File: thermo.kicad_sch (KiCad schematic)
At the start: 39 parts, among them J1 USB_C_Receptacle_USB2.0_14P, Q1 NPN, Q2 NPN, U1 ESP32-C6, U2 W25Q128JVS, U3 USBLC6-2SC6, Y1 40M, Y2 32k768

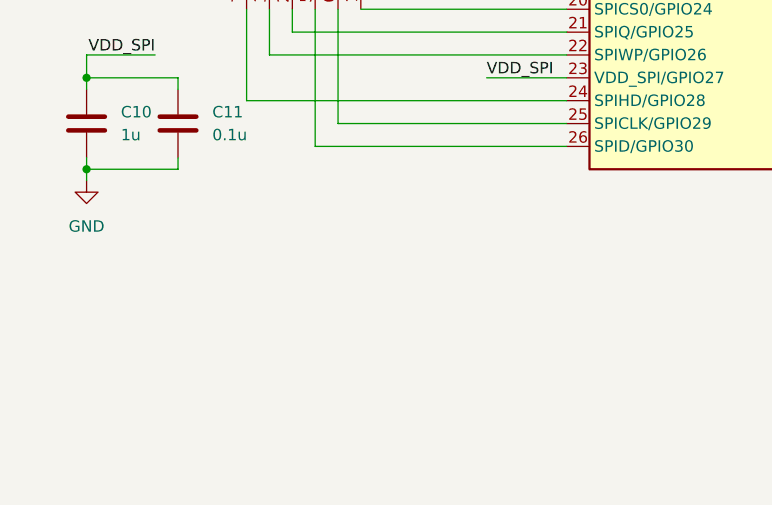
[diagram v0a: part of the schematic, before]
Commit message: add 5v to 3v3 ldo
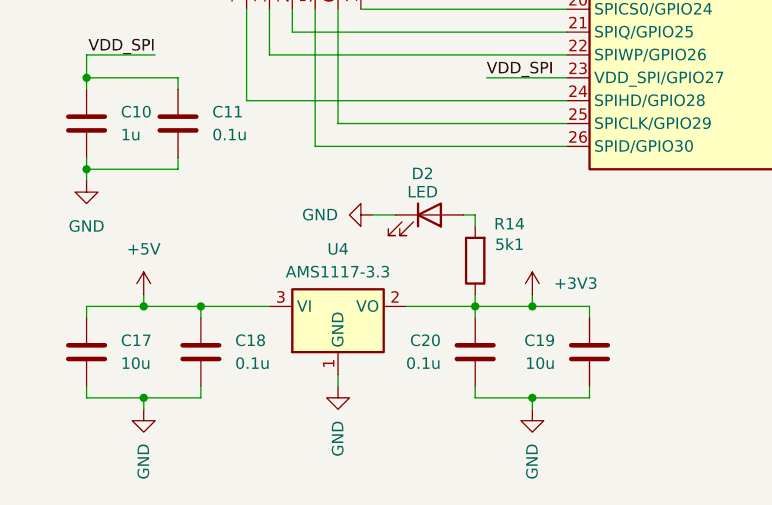
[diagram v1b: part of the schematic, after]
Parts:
- added C17, C19: 10u, symbol Device:C
- added C18, C20: 0.1u, symbol Device:C
- added D2: LED, symbol Device:LED
- added R14: 5k1, symbol Device:R
- added U4: AMS1117-3.3, Package_TO_SOT_SMD:SOT-223-3_TabPin2, symbol Regulator_Linear:AMS1117-3.3
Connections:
- net +3V3: now also C19.1, C20.1, R14.1, U4.2 (VO)
- net +5V: now also C17.1, C18.1, U4.3 (VI)
- net GND: now also C17.2, C18.2, C19.2, C20.2, D2.1 (K), U4.1 (GND)
- new net: D2.2 (A), R14.2

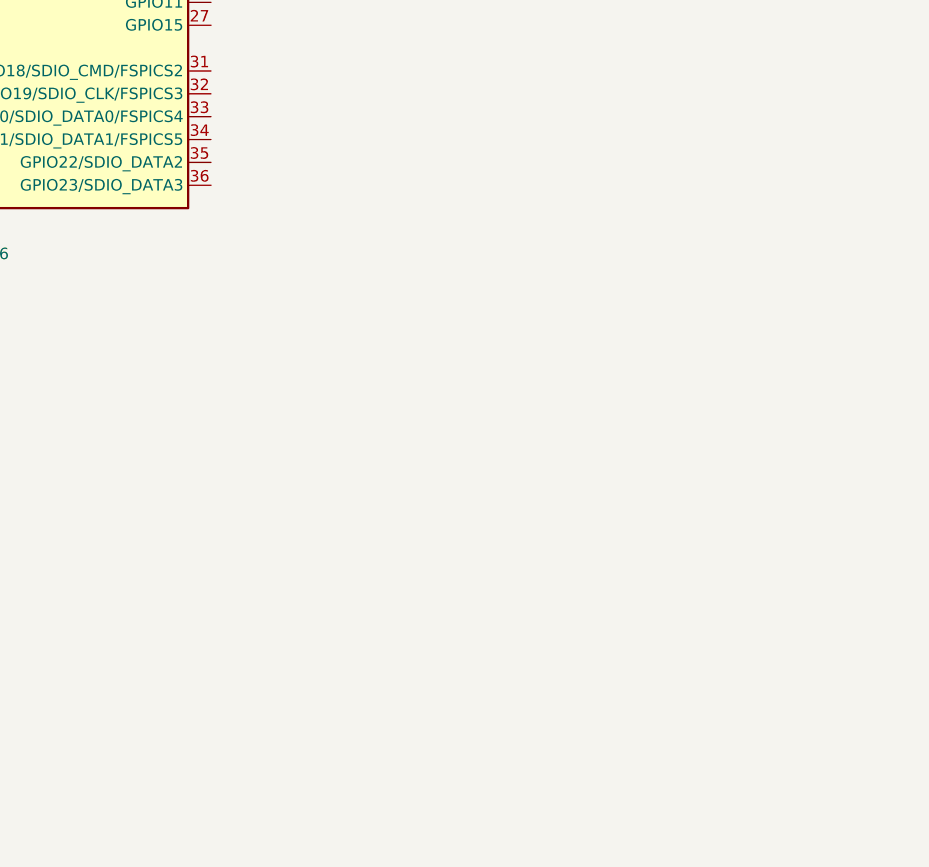
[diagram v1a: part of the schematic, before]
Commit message: add CP2102N usb to uart
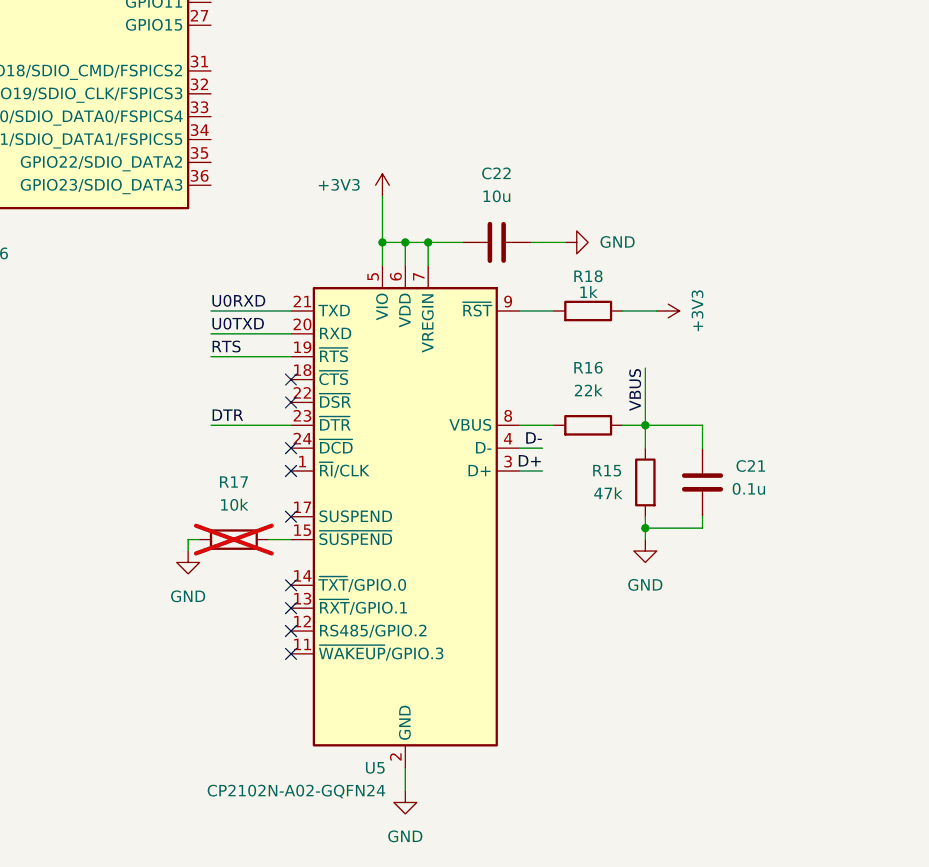
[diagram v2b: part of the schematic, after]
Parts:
- added C21: 0.1u, symbol Device:C
- added C22: 10u, symbol Device:C
- added R15: 47k, symbol Device:R
- added R16: 22k, symbol Device:R
- added R17: 10k, symbol Device:R
- added R18: 1k, symbol Device:R
- added U5: CP2102N-A02-GQFN24, Package_DFN_QFN:QFN-24-1EP_4x4mm_P0.5mm_EP2.6x2.6mm, symbol Interface_USB:CP2102N-Axx-xQFN24
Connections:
- net +3V3: now also C22.2, R18.1, U5.5 (VIO), U5.6 (VDD), U5.7 (VREGIN)
- net DTR: now also U5.23 (~{DTR})
- net GND: now also C21.2, C22.1, R15.2, R17.2, U5.2 (GND), U5.25 (GND)
- net RTS: now also U5.19 (~{RTS})
- net U0RXD: now also U5.21 (TXD)
- net U0TXD: now also U5.20 (RXD)
- net VBUS: now also C21.1, R15.1, R16.1
- new net: R16.2, U5.8 (VBUS)
- new net: R18.2, U5.9 (~{RST})
- new net: R17.1, U5.15 (~{SUSPEND})
- new net D+: U5.3 (D+)
- new net D-: U5.4 (D-)
- no-connect marks 0 -> 9

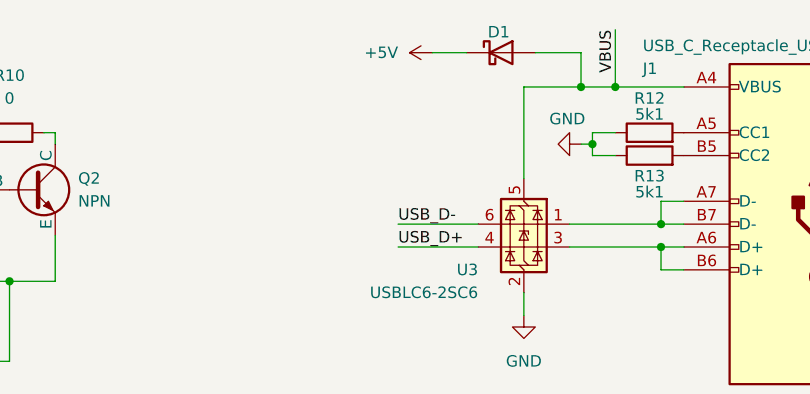
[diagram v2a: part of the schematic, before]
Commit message: add 10uF decoupling cap to usb connector VBUS
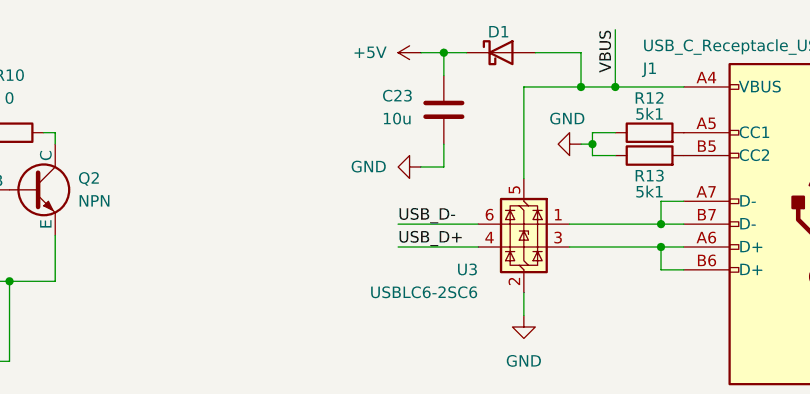
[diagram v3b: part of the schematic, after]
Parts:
- added C23: 10u, symbol Device:C
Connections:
- net +5V: now also C23.1
- net GND: now also C23.2
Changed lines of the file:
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@@
 	)
 	(junction
+		(at 229.87 16.51)
+		(diameter 0)
+		(color 0 0 0 0)
+	)
+	(junction
 		(at 90.17 20.32)
 		(diameter 0)
@@
 	(wire
 		(pts
+			(xy 227.33 29.21) (xy 229.87 29.21)
+		)
+		(stroke
+			(width 0)
+			(type default)
+		)
+	)
+	(wire
+		(pts
 			(xy 186.69 144.78) (xy 189.23 144.78)
 		)
@@
 	(wire
 		(pts
-			(xy 228.6 16.51) (xy 232.41 16.51)
+			(xy 227.33 16.51) (xy 229.87 16.51)
 		)
 		(stroke
@@
 	(wire
 		(pts
+			(xy 229.87 16.51) (xy 232.41 16.51)
+		)
+		(stroke
+			(width 0)
+			(type default)
+		)
+	)
+	(wire
+		(pts
 			(xy 21.59 120.65) (xy 21.59 121.92)
 		)
@@
 	(wire
 		(pts
+			(xy 229.87 16.51) (xy 229.87 19.05)
+		)
+		(stroke
+			(width 0)
+			(type default)
+		)
+	)
+	(wire
+		(pts
 			(xy 30.48 55.88) (xy 31.75 55.88)
 		)
@@
 	(wire
 		(pts
+			(xy 229.87 29.21) (xy 229.87 26.67)
+		)
+		(stroke
+			(width 0)
+			(type default)
+		)
+	)
+	(wire
+		(pts
 			(xy 189.23 154.94) (xy 189.23 156.21)
 		)
@@
 	)
 	(symbol
+		(lib_id "power:GND")
+		(at 227.33 29.21 270)
+		(unit 1)
+		(exclude_from_sim no)
+		(in_bom yes)
+		(on_board yes)
+		(dnp no)
+		(fields_autoplaced yes)
+		(property "Reference" "#PWR031"
+			(at 220.98 29.21 0)
+			(effects
+				(font
+					(size 1.27 1.27)
+				)
+				(hide yes)
+			)
+		)
+		(property "Value" "GND"
+			(at 223.52 29.2099 90)
+			(effects
+				(font
+					(size 1.27 1.27)
+				)
+				(justify right)
+			)
+		)
+		(property "Footprint" ""
+			(at 227.33 29.21 0)
+			(effects
+				(font
+					(size 1.27 1.27)
+				)
+				(hide yes)
+			)
+		)
+		(property "Datasheet" ""
+			(at 227.33 29.21 0)
+			(effects
+				(font
+					(size 1.27 1.27)
+				)
+				(hide yes)
+			)
+		)
+		(property "Description" "Power symbol creates a global label with name \"GND\" , ground"
+			(at 227.33 29.21 0)
+			(effects
+				(font
+					(size 1.27 1.27)
+				)
+				(hide yes)
+			)
+		)
+		(pin "1"
+		)
+		(instances
+			(project "thermo"
+				(path "/fde4d48d-460a-4d76-9ab6-1824c1ad585e"
+					(reference "#PWR031")
+					(unit 1)
+				)
+			)
+		)
+	)
+	(symbol
 		(lib_id "Device:R")
 		(at 252.73 25.4 90)
@@
 	(symbol
 		(lib_id "power:+5V")
-		(at 228.6 16.51 90)
+		(at 227.33 16.51 90)
 		(unit 1)
 		(exclude_from_sim no)
@@
 		(fields_autoplaced yes)
 		(property "Reference" "#PWR018"
-			(at 232.41 16.51 0)
+			(at 231.14 16.51 0)
 			(effects
 				(font
@@
 		)
 		(property "Value" "+5V"
-			(at 224.79 16.5099 90)
+			(at 223.52 16.5099 90)
 			(effects
 				(font
@@
 		)
 		(property "Footprint" ""
-			(at 228.6 16.51 0)
+			(at 227.33 16.51 0)
 			(effects
 				(font
@@
 		)
 		(property "Datasheet" ""
-			(at 228.6 16.51 0)
+			(at 227.33 16.51 0)
 			(effects
 				(font
@@
 		)
 		(property "Description" "Power symbol creates a global label with name \"+5V\""
-			(at 228.6 16.51 0)
+			(at 227.33 16.51 0)
 			(effects
 				(font
@@
 					(unit 1)
 				)
+			)
+		)
+	)
+	(symbol
+		(lib_id "Device:C")
+		(at 229.87 22.86 0)
+		(unit 1)
+		(exclude_from_sim no)
+		(in_bom yes)
+		(on_board yes)
+		(dnp no)
+		(property "Reference" "C23"
+			(at 223.012 21.336 0)
+			(effects
+				(font
+					(size 1.27 1.27)
+				)
+				(justify left)
+			)
+		)
+		(property "Value" "10u"
+			(at 223.012 23.876 0)
+			(effects
+				(font
+					(size 1.27 1.27)
+				)
+				(justify left)
+			)
+		)
+		(property "Footprint" ""
+			(at 230.8352 26.67 0)
+			(effects
+				(font
+					(size 1.27 1.27)
+				)
+				(hide yes)
+			)
+		)
+		(property "Datasheet" "~"
+			(at 229.87 22.86 0)
+			(effects
+				(font
+					(size 1.27 1.27)
+				)
+				(hide yes)
+			)
+		)
+		(property "Description" "Unpolarized capacitor"
+			(at 229.87 22.86 0)
+			(effects
+				(font
+					(size 1.27 1.27)
+				)
+				(hide yes)
+			)
+		)
+		(pin "1"
+		)
+		(pin "2"
+		)
+		(instances
+			(project ""
+				(path "/fde4d48d-460a-4d76-9ab6-1824c1ad585e"
+					(reference "C23")
+					(unit 1)
+				)

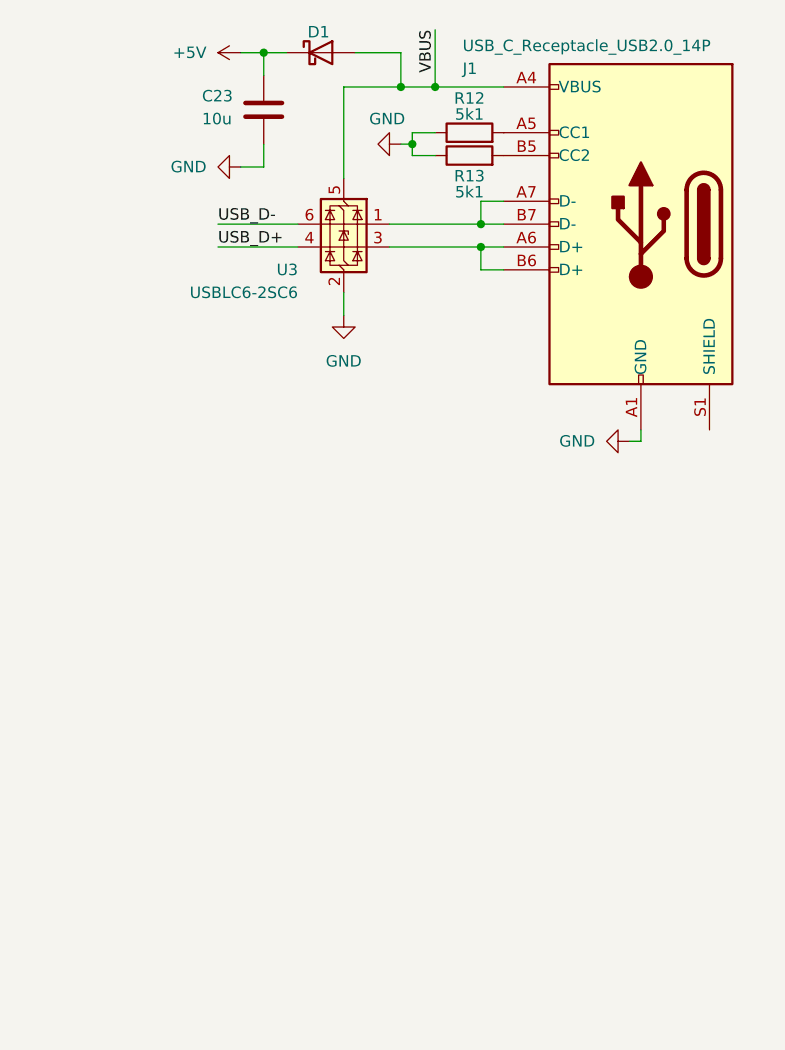
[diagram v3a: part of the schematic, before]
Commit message: add esp usb connector
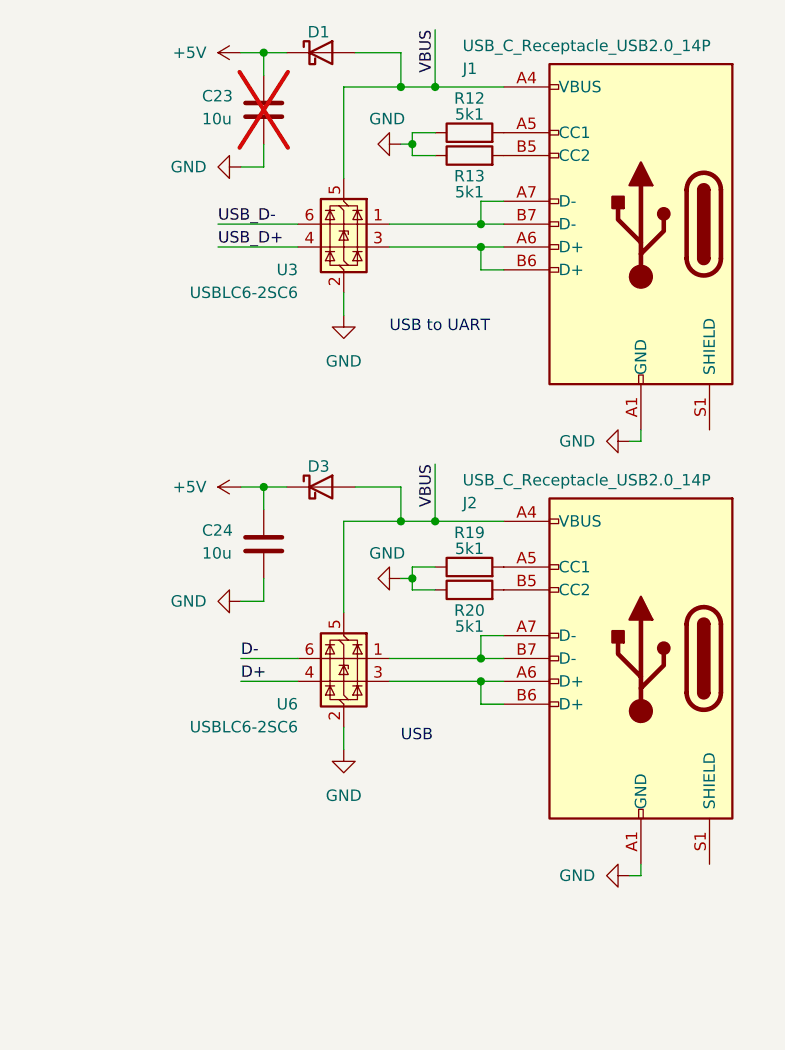
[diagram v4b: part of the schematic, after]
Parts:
- added C24: 10u, symbol Device:C
- added D3: D_Schottky, symbol Device:D_Schottky
- added J2: USB_C_Receptacle_USB2.0_14P, symbol Connector:USB_C_Receptacle_USB2.0_14P
- added R19, R20: 5k1, symbol Device:R
- added U6: USBLC6-2SC6, Package_TO_SOT_SMD:SOT-23-6, symbol Power_Protection:USBLC6-2SC6
- C23: now not fitted
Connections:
- net +5V: now also C24.1, D3.1 (K)
- net D+: now also U6.4 (I/O2)
- net D-: now also U6.6 (I/O1)
- net GND: now also C24.2, J2.A1 (GND), J2.A12 (GND), J2.B1 (GND), J2.B12 (GND), R19.1, R20.1, U6.2 (GND)
- net VBUS: now also D3.2 (A), J2.A4 (VBUS), J2.A9 (VBUS), J2.B4 (VBUS), J2.B9 (VBUS), U6.5 (VBUS)
- new net: J2.A7 (D-), J2.B7 (D-), U6.1 (I/O1)
- new net: J2.A6 (D+), J2.B6 (D+), U6.3 (I/O2)
- new net: J2.B5 (CC2), R20.2
- new net: J2.A5 (CC1), R19.2
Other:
- note added: "USB"
- note added: "USB to UART"

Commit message: add rst and boot buttons
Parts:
- added SW1, SW2: SW_Push, symbol Switch:SW_Push
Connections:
- net CHIP_PU: now also SW2.2
- net GND: now also SW1.1, SW2.1
- net GPIO9: now also SW1.2

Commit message: add bme280 sensor
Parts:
- added C25, C26: 0.1u, symbol Device:C
- added R21, R22: 2k4, symbol Device:R
- added U7: BME280, Package_LGA:Bosch_LGA-8_2.5x2.5mm_P0.65mm_ClockwisePinNumbering, symbol Sensor:BME280
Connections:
- net +3V3: now also C25.1, C26.1, R21.2, R22.2, U7.2 (CSB), U7.6 (VDDIO), U7.8 (VDD)
- net GND: now also C25.2, C26.2, U7.1 (GND), U7.5 (SDO), U7.7 (GND)
- net GPIO18: now reaches U1.31 (GPIO18/SDIO_CMD/FSPICS2)
- net GPIO18: now also R22.1, U7.4 (SCK)
- net GPIO19: now reaches U1.32 (GPIO19/SDIO_CLK/FSPICS3)
- net GPIO19: now also R21.1, U7.3 (SDI)
